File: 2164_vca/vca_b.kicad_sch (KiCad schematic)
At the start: 27 parts, among them J11 CV B, J12 To J3, J13 Conn_01x03_Pin, J14 To J3, J15 Conn_01x03_Pin, J16 In B, J17 Out B, J18 To J3, J19 Conn_01x03_Pin, U2 TL074

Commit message: 2164 vca: assigned missing footprints and some tweaks
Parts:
- RV8: footprint (none) -> Potentiometer_THT:Potentiometer_Runtron_RM-065_Vertical
- RV9: value B10K -> B50K; footprint (none) -> Potentiometer_THT:Potentiometer_Runtron_RM-065_Vertical
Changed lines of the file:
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@@
+		)
+	)
+	(global_label "VCA3_CV"
+		(shape input)
+		(at 96.52 165.1 90)
+		(fields_autoplaced yes)
+		(effects
+			(font
+				(size 1.27 1.27)
+			)
+			(justify left)
+		)
+		(property "Intersheetrefs" "${INTERSHEET_REFS}"
+			(at 96.52 154.1319 90)
+			(effects
+				(font
+					(size 1.27 1.27)
+				)
+				(justify left)
+				(hide yes)
+			)
+		)
+	)
+	(global_label "VCA3_IN"
+		(shape input)
+		(at 83.82 151.13 0)
+		(fields_autoplaced yes)
+		(effects
+			(font
+				(size 1.27 1.27)
+			)
+			(justify left)
+		)
+		(property "Intersheetrefs" "${INTERSHEET_REFS}"
+			(at 94.3648 151.13 0)
+			(effects
+				(font
+					(size 1.27 1.27)
+				)
+				(justify left)
+				(hide yes)
+			)
 		)
 	)
@@
 		)
 	)
+	(global_label "VCA4_CV"
+		(shape input)
+		(at 175.26 114.3 270)
+		(fields_autoplaced yes)
+		(effects
+			(font
+				(size 1.27 1.27)
+			)
+			(justify right)
+		)
+		(property "Intersheetrefs" "${INTERSHEET_REFS}"
+			(at 175.26 125.2681 90)
+			(effects
+				(font
+					(size 1.27 1.27)
+				)
+				(justify right)
+				(hide yes)
+			)
+		)
+	)
+	(global_label "VCA3_OUT"
+		(shape input)
+		(at 110.49 151.13 180)
+		(fields_autoplaced yes)
+		(effects
+			(font
+				(size 1.27 1.27)
+			)
+			(justify right)
+		)
+		(property "Intersheetrefs" "${INTERSHEET_REFS}"
+			(at 98.2519 151.13 0)
+			(effects
+				(font
+					(size 1.27 1.27)
+				)
+				(justify right)
+				(hide yes)
+			)
+		)
+	)
+	(global_label "VCA4_IN"
+		(shape input)
+		(at 162.56 128.27 0)
+		(fields_autoplaced yes)
+		(effects
+			(font
+				(size 1.27 1.27)
+			)
+			(justify left)
+		)
+		(property "Intersheetrefs" "${INTERSHEET_REFS}"
+			(at 173.1048 128.27 0)
+			(effects
+				(font
+					(size 1.27 1.27)
+				)
+				(justify left)
+				(hide yes)
+			)
+		)
+	)
 	(global_label "CTRL_GND"
 		(shape passive)
@@
 		)
 	)
+	(global_label "VCA4_OUT"
+		(shape input)
+		(at 189.23 128.27 180)
+		(fields_autoplaced yes)
+		(effects
+			(font
+				(size 1.27 1.27)
+			)
+			(justify right)
+		)
+		(property "Intersheetrefs" "${INTERSHEET_REFS}"
+			(at 176.9919 128.27 0)
+			(effects
+				(font
+					(size 1.27 1.27)
+				)
+				(justify right)
+				(hide yes)
+			)
+		)
+	)
 	(global_label "CTRL_GND"
 		(shape passive)
@@
 				(hide yes)
 			)
-		)
-	)
-	(hierarchical_label "VCA4_CV"
-		(shape input)
-		(at 175.26 114.3 270)
-		(effects
-			(font
-				(size 1.27 1.27)
-			)
-			(justify right)
-		)
-	)
-	(hierarchical_label "VCA4_OUT"
-		(shape input)
-		(at 189.23 128.27 180)
-		(effects
-			(font
-				(size 1.27 1.27)
-			)
-			(justify right)
-		)
-	)
-	(hierarchical_label "VCA3_CV"
-		(shape input)
-		(at 96.52 165.1 90)
-		(effects
-			(font
-				(size 1.27 1.27)
-			)
-			(justify left)
-		)
-	)
-	(hierarchical_label "VCA3_OUT"
-		(shape input)
-		(at 110.49 151.13 180)
-		(effects
-			(font
-				(size 1.27 1.27)
-			)
-			(justify right)
-		)
-	)
-	(hierarchical_label "VCA3_IN"
-		(shape input)
-		(at 83.82 151.13 0)
-		(effects
-			(font
-				(size 1.27 1.27)
-			)
-			(justify left)
-		)
-	)
-	(hierarchical_label "VCA4_IN"
-		(shape input)
-		(at 162.56 128.27 0)
-		(effects
-			(font
-				(size 1.27 1.27)
-			)
-			(justify left)
 		)
 	)
@@
 			)
 		)
-		(property "Value" "B10K"
+		(property "Value" "B50K"
 			(at 60.96 152.3999 0)
 			(effects
@@
 			)
 		)
-		(property "Footprint" ""
+		(property "Footprint" "Potentiometer_THT:Potentiometer_Runtron_RM-065_Vertical"
 			(at 63.5 151.13 0)
 			(effects
@@
 			)
 		)
-		(property "Footprint" ""
+		(property "Footprint" "Potentiometer_THT:Potentiometer_Runtron_RM-065_Vertical"
 			(at 63.5 120.65 0)
 			(effects

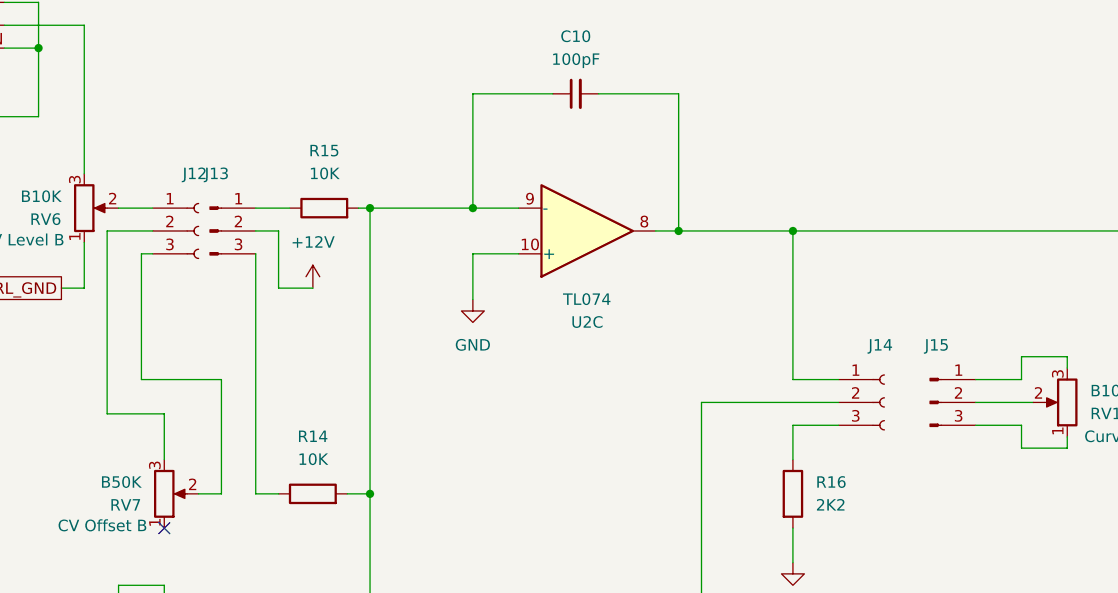
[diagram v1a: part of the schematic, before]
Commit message: 2164 vca: finalized panel and control board layout
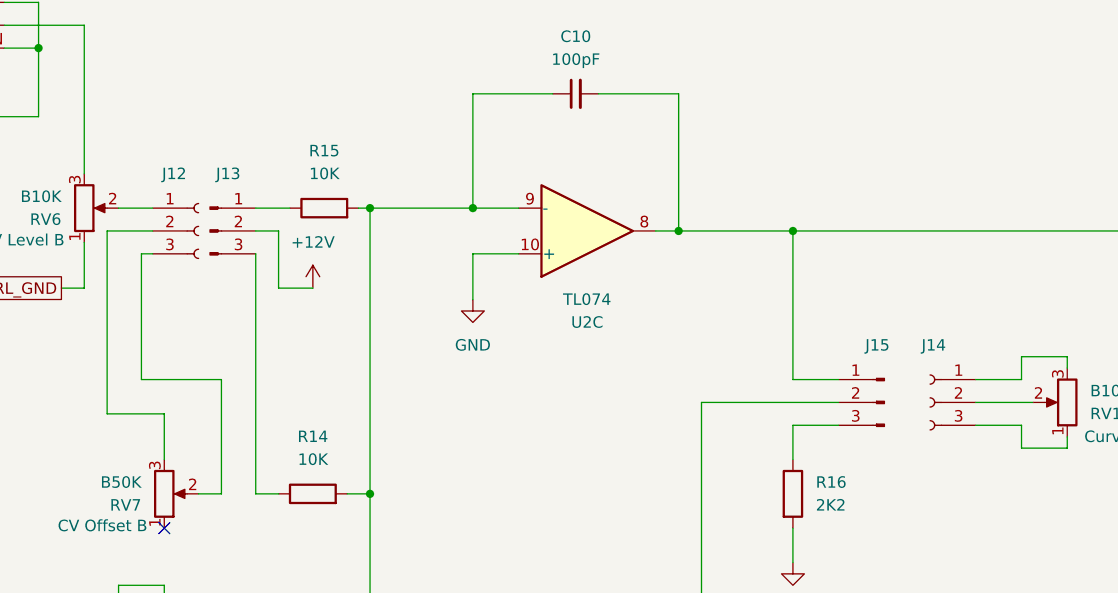
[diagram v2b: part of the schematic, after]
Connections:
- net VCA3_CV: now also J15.2 (Pin_2); no longer J14.2 (Pin_2)
- net VCA4_CV: now also J15.1 (Pin_1); no longer J14.1 (Pin_1)
- net at RV10.3: now also J14.1 (Pin_1); no longer J15.1 (Pin_1)
- net at RV10.2: now also J14.2 (Pin_2); no longer J15.2 (Pin_2)
- net at J15.3 (Pin_3): now also R16.1; no longer RV10.1
- net at J14.3 (Pin_3): now also RV10.1; no longer R16.1
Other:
- moved on the sheet: J14, J15
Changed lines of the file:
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@@
 	(symbol
 		(lib_id "Connector:Conn_01x03_Pin")
-		(at 148.59 86.36 0)
+		(at 143.51 86.36 0)
+		(mirror y)
 		(unit 1)
 		(exclude_from_sim no)
@@
 		(dnp no)
 		(property "Reference" "J15"
-			(at 149.352 80.01 0)
+			(at 142.748 80.01 0)
 			(effects
 				(font
@@
 		)
 		(property "Value" "Conn_01x03_Pin"
-			(at 149.225 81.28 0)
+			(at 142.875 81.28 0)
 			(effects
 				(font
@@
 		)
 		(property "Footprint" "Connector_PinHeader_2.54mm:PinHeader_1x03_P2.54mm_Vertical"
-			(at 148.59 86.36 0)
+			(at 143.51 86.36 0)
 			(effects
 				(font
@@
 		)
 		(property "Datasheet" "~"
-			(at 148.59 86.36 0)
+			(at 143.51 86.36 0)
 			(effects
 				(font
@@
 		)
 		(property "Description" "Generic connector, single row, 01x03, script generated"
-			(at 148.59 86.36 0)
+			(at 143.51 86.36 0)
 			(effects
 				(font
@@
 	(symbol
 		(lib_id "Connector:Conn_01x03_Socket")
-		(at 143.51 86.36 0)
+		(at 148.59 86.36 0)
+		(mirror y)
 		(unit 1)
 		(exclude_from_sim no)
@@
 		(dnp no)
 		(property "Reference" "J14"
-			(at 141.732 80.01 0)
+			(at 150.368 80.01 0)
 			(effects
 				(font
@@
 		)
 		(property "Value" "To J3"
-			(at 144.78 87.6299 0)
+			(at 147.32 87.6299 0)
 			(effects
 				(font
@@
 		)
 		(property "Footprint" "Connector_PinSocket_2.54mm:PinSocket_1x03_P2.54mm_Vertical"
-			(at 143.51 86.36 0)
+			(at 148.59 86.36 0)
 			(effects
 				(font
@@
 		)
 		(property "Datasheet" "~"
-			(at 143.51 86.36 0)
+			(at 148.59 86.36 0)
 			(effects
 				(font
@@
 		)
 		(property "Description" "Generic connector, single row, 01x03, script generated"
-			(at 143.51 86.36 0)
+			(at 148.59 86.36 0)
 			(effects
 				(font
@@
 		(dnp no)
 		(property "Reference" "J12"
-			(at 65.532 60.96 0)
+			(at 63.246 60.96 0)
 			(effects
 				(font
@@
 		(dnp no)
 		(property "Reference" "J13"
-			(at 69.342 60.96 0)
-			(effects
-				(font
+			(at 70.612 60.96 0)
+			(effects
+				(font
